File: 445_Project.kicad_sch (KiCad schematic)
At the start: 22 parts, among them J1 SM02B-SRSS-TB_LF__SN_, J10 105164-0001, J2 69167-107HLF, J3 69167-107HLF, J4 69167-114HLF, J5 69167-114HLF, J6 69167-107HLF, J7 69167-107HLF, J8 SM02B-SRSS-TB_LF__SN_, J9 105164-0001, U1 ESP32-S3-WROOM-1-N16R8, U10 LP2950CZ-3.3_LFT3, U2 ESP32-S3-WROOM-1-N16R8, U3 LSM6DSMTR, U4 LSM6DSMTR, U5 LSM6DSMTR, U6 LSM6DSMTR, U7 LSM6DSMTR, U8 LSM6DSMTR, U9 LP2950CZ-3.3_LFT3

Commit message: enable signal and analog switches
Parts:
- added C1, C10, C11, C12, C2, C3, C4, C5, C6, C7, C8, C9: 100nF, symbol Device:C_Small
- added R1, R2: 10k, symbol Device:R
- added U11, U12, U13, U14: TS3A5018D, TS3A5018D:SOIC127P600X175-16N, symbol TS3A5018D:TS3A5018D
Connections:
- net +3.3V: now also U1.3 (EN), U2.3 (EN), U3.5 (VDDIO), U4.5 (VDDIO), U5.5 (VDDIO), U6.5 (VDDIO), U7.5 (VDDIO), U8.5 (VDDIO), C1.1, C10.2, C11.1, C12.2, C2.2, C3.1, C4.2, C5.1, C6.2, C7.1, C8.2, C9.1, R1.1, R2.1, U11.16 (VCC), U12.16 (VCC), U13.16 (VCC), U14.16 (VCC)
- net CLK: now also U11.7 (COM2), U12.7 (COM2), U13.7 (COM2), U14.7 (COM2); no longer J2.06, J3.06, J4.06, J4.13, J5.06, J5.13, J6.06, J7.06, U3.13 (SCL/SPC), U4.13 (SCL/SPC), U5.13 (SCL/SPC), U6.13 (SCL/SPC), U7.13 (SCL/SPC), U8.13 (SCL/SPC)
- net CS1: now also U1.18 (IO10), U2.18 (IO10), U11.15 (~{EN}), U11.4 (COM1), U13.15 (~{EN}), U13.4 (COM1); no longer U1.23 (IO21), U2.23 (IO21), U4.12 (CS), U7.12 (CS)
- net CS2: now also U1.23 (IO21), U2.23 (IO21), U12.15 (~{EN}), U12.4 (COM1), U14.15 (~{EN}), U14.4 (COM1); no longer J4.07, J5.07, J6.07, J7.07, U1.24 (IO47), U2.24 (IO47), U5.12 (CS), U8.12 (CS)
- net GND: now also U7.2 (SDX), C1.2, C10.1, C11.2, C12.1, C2.1, C3.2, C4.1, C5.2, C6.1, C7.2, C8.1, C9.2, R1.2, R2.2, U11.8 (GND), U12.8 (GND), U13.8 (GND), U14.8 (GND)
- net MISO: now also U11.12 (COM4), U12.12 (COM4), U13.12 (COM4), U14.12 (COM4); no longer J2.04, J3.04, J4.04, J4.11, J5.04, J5.11, J6.04, J7.04, U3.1 (SDO/SA0), U4.1 (SDO/SA0), U5.1 (SDO/SA0), U6.1 (SDO/SA0), U7.1 (SDO/SA0), U8.1 (SDO/SA0)
- net MOSI: now also U11.9 (COM3), U12.9 (COM3), U13.9 (COM3), U14.9 (COM3); no longer J2.05, J3.05, J4.05, J4.12, J5.05, J5.12, J6.05, J7.05, U3.14 (SDA/SDI/SDO), U4.14 (SDA/SDI/SDO), U5.14 (SDA/SDI/SDO), U6.14 (SDA/SDI/SDO), U7.14 (SDA/SDI/SDO), U8.14 (SDA/SDI/SDO)
- net CS0 renamed SENSOR_1
- net SENSOR_1: now also U11.3 (NO1), U13.3 (NO1); no longer U1.18 (IO10), U2.18 (IO10)
- new net CLK1: J2.06, J3.06, J4.13, J5.13, U11.6 (NO2), U13.6 (NO2), U3.13 (SCL/SPC), U6.13 (SCL/SPC)
- new net CLK2: U11.5 (NC2), U13.5 (NC2), U4.13 (SCL/SPC), U7.13 (SCL/SPC)
- new net CLK3: J4.06, J5.06, J6.06, J7.06, U12.6 (NO2), U14.6 (NO2), U5.13 (SCL/SPC), U8.13 (SCL/SPC)
- new net MISO_1: J2.04, J3.04, J4.11, J5.11, U11.13 (NO4), U13.13 (NO4), U3.1 (SDO/SA0), U6.1 (SDO/SA0)
- new net MISO_2: U11.14 (NC4), U13.14 (NC4), U4.1 (SDO/SA0), U7.1 (SDO/SA0)
- new net MISO_3: J4.04, J5.04, J6.04, J7.04, U12.13 (NO4), U14.13 (NO4), U5.1 (SDO/SA0), U8.1 (SDO/SA0)
- new net MOSI_1: J2.05, J3.05, J4.12, J5.12, U11.10 (NO3), U13.10 (NO3), U3.14 (SDA/SDI/SDO), U6.14 (SDA/SDI/SDO)
- new net MOSI_2: U11.11 (NC3), U13.11 (NC3), U4.14 (SDA/SDI/SDO), U7.14 (SDA/SDI/SDO)
- new net MOSI_3: J4.05, J5.05, J6.05, J7.05, U12.10 (NO3), U14.10 (NO3), U5.14 (SDA/SDI/SDO), U8.14 (SDA/SDI/SDO)
- new net SENSOR_2: U11.2 (NC1), U13.2 (NC1), U4.12 (CS), U7.12 (CS)
- new net SENSOR_3: J4.07, J5.07, J6.07, J7.07, U12.3 (NO1), U14.3 (NO1), U5.12 (CS), U8.12 (CS)
- new net SENSOR_SEL: U1.24 (IO47), U11.1 (IN), U12.1 (IN), U13.1 (IN), U14.1 (IN), U2.24 (IO47)
- no-connect marks 0 -> 98
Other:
- moved on the sheet: J1, J10, J2, J3, J4, J5, J6, J7, J8, J9, U10, U3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

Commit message: replace bicep connector and add int1 connections
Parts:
- removed J4, J5: 69167-114HLF, 69167-114HLF:AMPHENOL_69167-114HLF, symbol 69167-114HLF:69167-114HLF
- added J11, J12, J4, J5: 69167-107HLF, 69167-107HLF:AMPHENOL_69167-107HLF, symbol 69167-107HLF:69167-107HLF
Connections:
- net +3.3V: now also J11.01, J12.01, J4.01, J5.01
- net CLK1: now also J4.06, J5.06
- net CLK3: now also J11.06, J12.06
- net GND: now also J11.02, J12.02, J4.02, J5.02
- net MISO_1: now also J4.04, J5.04
- net MISO_3: now also J11.04, J12.04
- net MOSI_1: now also J4.05, J5.05
- net MOSI_3: now also J11.05, J12.05
- net SENSOR_1: now also J4.07, J5.07
- net SENSOR_3: now also J11.07, J12.07
- net INT1_3: now reaches J6.03
- net INT1_3: now also J7.03, U1.10 (IO17), U2.10 (IO17), U5.4 (INT1), U8.4 (INT1), J11.03, J12.03
- net INT1_1: now reaches U6.4 (INT1)
- net INT1_1: now also J2.03, J3.03, U1.8 (IO15), U2.8 (IO15), U3.4 (INT1), J4.03, J5.03
- net INT1_2: now reaches U4.4 (INT1)
- net INT1_2: now also U1.9 (IO16), U2.9 (IO16)
- no-connect marks 98 -> 79

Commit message: Layout First Draft
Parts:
- removed J10, J9: 105164-0001, 105164-0001:MOLEX_105164-0001, symbol 105164-0001:105164-0001
- added J10, J9: 87583-2010RPLF, 87583-2010RPLF:AMPHENOL_87583-2010RPLF, symbol 87583-2010RPLF:87583-2010RPLF
- C1, C10, C11, C12, C2, C3, C4, C5, C6, C7, C8, C9: footprint (none) -> CL21F104ZAANNNC:CAPC2012X135N
- R1, R2: footprint (none) -> RMCF0805JG10K0:RESC2012X65N
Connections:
- net 3.3V is gone; now on net +3.3V: U1.2 (3V3), U10.1 (OUT), U2.2 (3V3), U9.1 (OUT)
- net +3.3V: now also J10.01 (VCC), J9.01 (VCC)
- net D+: now also J10.03 (D+), J9.03 (D+)
- net D-: now also J10.02 (D-), J9.02 (D-)
- net GND: now also J10.04 (GND), J9.04 (GND)
- net MISO: now also U1.19 (IO11), U2.19 (IO11); no longer U1.21 (IO13), U2.21 (IO13)
- net MOSI: now also U1.21 (IO13), U2.21 (IO13); no longer U1.19 (IO11), U2.19 (IO11)
- new net: J10.S1 (SHIELD), J10.S2 (SHIELD)
- new net: J9.S1 (SHIELD), J9.S2 (SHIELD)
- no-connect marks 79 -> 77

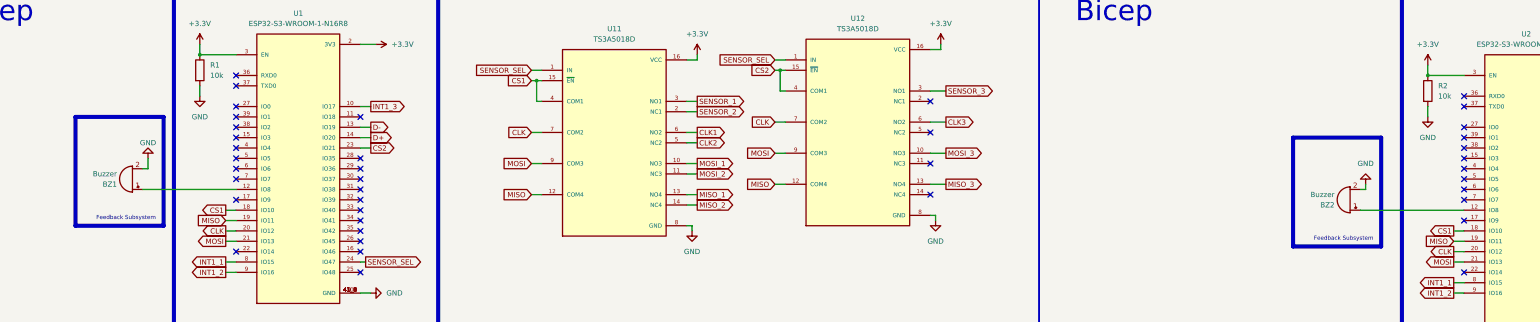
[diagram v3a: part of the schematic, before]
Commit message: adding buzzer
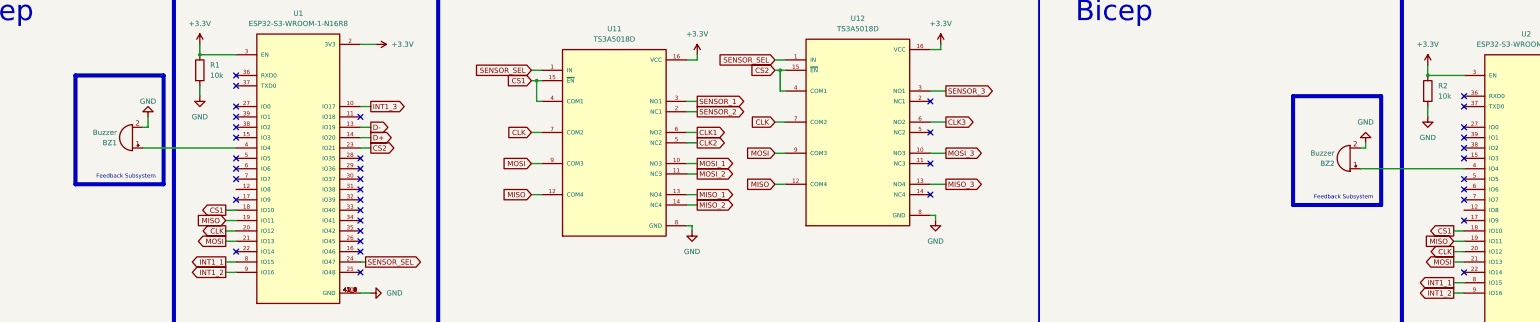
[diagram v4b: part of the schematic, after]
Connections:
- net at BZ1.1 (+): now also U1.4 (IO4); no longer U1.12 (IO8)
- net at U2.12 (IO8): no longer BZ2.1 (+)
- net at U2.4 (IO4): now also BZ2.1 (+)
- no-connect marks 77 -> 75
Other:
- moved on the sheet: BZ1, BZ2
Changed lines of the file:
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@@
   (no_connect (at 78.74 196.85))
   (no_connect (at 88.9 76.2))
-  (no_connect (at 389.89 86.36))
   (no_connect (at 119.38 91.44))
   (no_connect (at 389.89 91.44))
@@
   (no_connect (at 259.08 69.85))
   (no_connect (at 259.08 77.47))
-  (no_connect (at 88.9 81.28))
   (no_connect (at 88.9 71.12))
   (no_connect (at 420.37 116.84))
@@
     (stroke (width 0) (type default))
   )
+  (wire (pts (xy 66.04 81.28) (xy 88.9 81.28))
+    (stroke (width 0) (type default))
+  )
   (wire (pts (xy 35.56 172.72) (xy 38.1 172.72))
     (stroke (width 0) (type default))
@@
     (stroke (width 0) (type default))
   )
-  (wire (pts (xy 365.76 90.17) (xy 365.76 91.44))
+  (wire (pts (xy 365.76 80.01) (xy 365.76 81.28))
     (stroke (width 0) (type default))
   )
@@
     (stroke (width 0) (type default))
   )
-  (wire (pts (xy 365.76 91.44) (xy 364.49 91.44))
+  (wire (pts (xy 365.76 81.28) (xy 364.49 81.28))
     (stroke (width 0) (type default))
   )
@@
     (stroke (width 0) (type default))
   )
-  (wire (pts (xy 67.31 83.82) (xy 67.31 86.36))
+  (wire (pts (xy 67.31 73.66) (xy 67.31 76.2))
     (stroke (width 0) (type default))
   )
@@
     (stroke (width 0) (type default))
   )
-  (wire (pts (xy 364.49 96.52) (xy 389.89 96.52))
-    (stroke (width 0) (type default))
-  )
   (wire (pts (xy 129.54 365.76) (xy 129.54 367.03))
     (stroke (width 0) (type default))
@@
     (stroke (width 0) (type default))
   )
-  (wire (pts (xy 66.04 91.44) (xy 88.9 91.44))
-    (stroke (width 0) (type default))
-  )
   (wire (pts (xy 222.25 62.23) (xy 222.25 67.31))
     (stroke (width 0) (type default))
@@
     (stroke (width 0) (type default))
   )
+  (wire (pts (xy 364.49 86.36) (xy 389.89 86.36))
+    (stroke (width 0) (type default))
+  )
   (wire (pts (xy 35.56 203.2) (xy 38.1 203.2))
     (stroke (width 0) (type default))
@@
     (stroke (width 0) (type default))
   )
-  (wire (pts (xy 67.31 86.36) (xy 66.04 86.36))
+  (wire (pts (xy 67.31 76.2) (xy 66.04 76.2))
     (stroke (width 0) (type default))
   )
@@
     (fill (type none))
   )
-  (rectangle (start 49.53 73.66) (end 71.12 100.33)
+  (rectangle (start 49.53 63.5) (end 71.12 90.17)
     (stroke (width 1) (type default) (color 127 0 255 1))
     (fill (type none))
   )
-  (rectangle (start 347.98 78.74) (end 369.57 105.41)
+  (rectangle (start 347.98 68.58) (end 369.57 95.25)
     (stroke (width 1) (type default) (color 127 0 255 1))
     (fill (type none))
@@
     (effects (font (size 2 2) (color 69 75 27 1)) (justify left bottom))
   )
-  (text "Feedback Subsystem" (at 353.06 104.14 0)
+  (text "Feedback Subsystem" (at 353.06 93.98 0)
     (effects (font (size 1 1) (color 127 0 255 1)) (justify left bottom))
   )
-  (text "Feedback Subsystem" (at 54.61 99.06 0)
+  (text "Feedback Subsystem" (at 54.61 88.9 0)
     (effects (font (size 1 1) (color 127 0 255 1)) (justify left bottom))
   )
@@
     )
   )
-  (symbol (lib_id "Device:Buzzer") (at 63.5 88.9 180) (unit 1)
+  (symbol (lib_id "Device:Buzzer") (at 63.5 78.74 180) (unit 1)
     (in_bom yes) (on_board yes) (dnp no) (fields_autoplaced)
-    (property "Reference" "BZ1" (at 59.69 90.17 0)
+    (property "Reference" "BZ1" (at 59.69 80.01 0)
       (effects (font (size 1.27 1.27)) (justify left))
     )
-    (property "Value" "Buzzer" (at 59.69 87.63 0)
+    (property "Value" "Buzzer" (at 59.69 77.47 0)
       (effects (font (size 1.27 1.27)) (justify left))
     )
-    (property "Footprint" "ECE 445 Footprints:AC-903-D-1P" (at 64.135 91.44 90)
+    (property "Footprint" "ECE 445 Footprints:AC-903-D-1P" (at 64.135 81.28 90)
       (effects (font (size 1.27 1.27)) hide)
     )
-    (property "Datasheet" "~" (at 64.135 91.44 90)
+    (property "Datasheet" "~" (at 64.135 81.28 90)
       (effects (font (size 1.27 1.27)) hide)
     )
@@
     )
   )
-  (symbol (lib_id "power:GND") (at 67.31 83.82 180) (unit 1)
+  (symbol (lib_id "power:GND") (at 67.31 73.66 180) (unit 1)
     (in_bom yes) (on_board yes) (dnp no)
-    (property "Reference" "#PWR022" (at 67.31 77.47 0)
+    (property "Reference" "#PWR022" (at 67.31 67.31 0)
       (effects (font (size 1.27 1.27)) hide)
     )
-    (property "Value" "GND" (at 67.31 80.01 0)
+    (property "Value" "GND" (at 67.31 69.85 0)
       (effects (font (size 1.27 1.27)))
     )
-    (property "Footprint" "" (at 67.31 83.82 0)
+    (property "Footprint" "" (at 67.31 73.66 0)
       (effects (font (size 1.27 1.27)) hide)
     )
-    (property "Datasheet" "" (at 67.31 83.82 0)
+    (property "Datasheet" "" (at 67.31 73.66 0)
       (effects (font (size 1.27 1.27)) hide)
     )
@@
     )
   )
-  (symbol (lib_id "power:GND") (at 365.76 90.17 180) (unit 1)
+  (symbol (lib_id "power:GND") (at 365.76 80.01 180) (unit 1)
     (in_bom yes) (on_board yes) (dnp no) (fields_autoplaced)
-    (property "Reference" "#PWR036" (at 365.76 83.82 0)
+    (property "Reference" "#PWR036" (at 365.76 73.66 0)
       (effects (font (size 1.27 1.27)) hide)
     )
-    (property "Value" "GND" (at 365.76 85.09 0)
+    (property "Value" "GND" (at 365.76 74.93 0)
       (effects (font (size 1.27 1.27)))
     )
-    (property "Footprint" "" (at 365.76 90.17 0)
+    (property "Footprint" "" (at 365.76 80.01 0)
       (effects (font (size 1.27 1.27)) hide)
     )
-    (property "Datasheet" "" (at 365.76 90.17 0)
+    (property "Datasheet" "" (at 365.76 80.01 0)
       (effects (font (size 1.27 1.27)) hide)
     )
@@
     )
   )
-  (symbol (lib_id "Device:Buzzer") (at 361.95 93.98 180) (unit 1)
+  (symbol (lib_id "Device:Buzzer") (at 361.95 83.82 180) (unit 1)
     (in_bom yes) (on_board yes) (dnp no) (fields_autoplaced)
-    (property "Reference" "BZ2" (at 358.14 95.25 0)
+    (property "Reference" "BZ2" (at 358.14 85.09 0)
       (effects (font (size 1.27 1.27)) (justify left))
     )
-    (property "Value" "Buzzer" (at 358.14 92.71 0)
+    (property "Value" "Buzzer" (at 358.14 82.55 0)
       (effects (font (size 1.27 1.27)) (justify left))
     )
-    (property "Footprint" "ECE 445 Footprints:AC-903-D-1P" (at 362.585 96.52 90)
+    (property "Footprint" "ECE 445 Footprints:AC-903-D-1P" (at 362.585 86.36 90)
       (effects (font (size 1.27 1.27)) hide)
     )
-    (property "Datasheet" "~" (at 362.585 96.52 90)
+    (property "Datasheet" "~" (at 362.585 86.36 90)
       (effects (font (size 1.27 1.27)) hide)
     )

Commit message: Edits 3/12
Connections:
- no-connect marks 75 -> 77
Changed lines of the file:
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@@
   (no_connect (at 78.74 196.85))
   (no_connect (at 88.9 76.2))
+  (no_connect (at 389.89 96.52))
   (no_connect (at 119.38 91.44))
   (no_connect (at 389.89 91.44))
@@
   (no_connect (at 389.89 88.9))
   (no_connect (at 88.9 73.66))
+  (no_connect (at 88.9 91.44))
   (no_connect (at 420.37 96.52))
   (no_connect (at 88.9 78.74))
